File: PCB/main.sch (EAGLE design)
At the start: 18 parts, among them IC1 DCDC, IC2 A4988BREAKOUT, IC3 A4988BREAKOUT, M1 NEAM17, M2 NEAM17

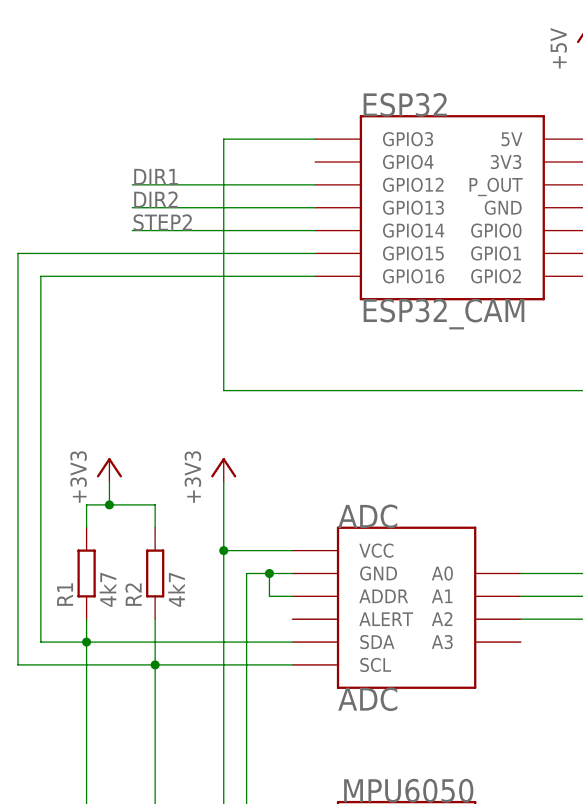
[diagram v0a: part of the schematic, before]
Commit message: PIN 16 is used by PSRAM ...
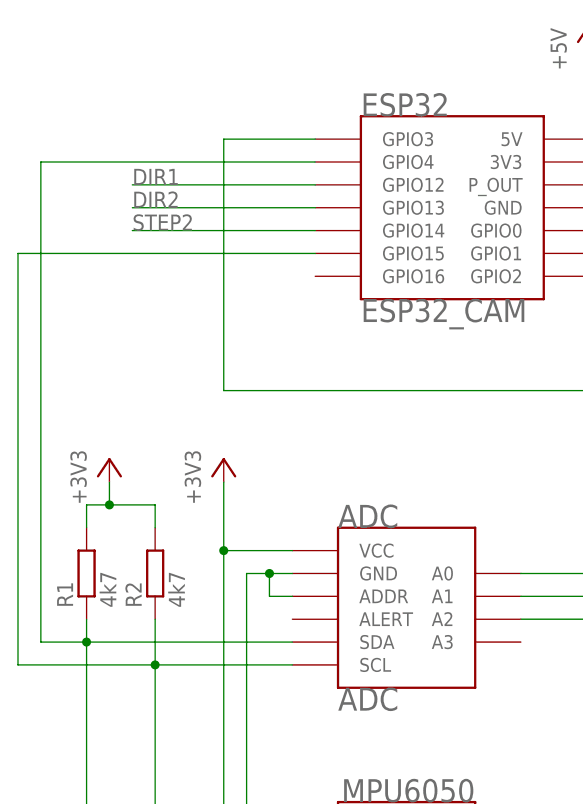
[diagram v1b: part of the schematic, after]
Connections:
- net N$19: now also ESP32.GPIO4; no longer ESP32.GPIO16
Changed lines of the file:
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@@
 <junction x="15.24" y="83.82"/>
 <wire x1="15.24" y1="83.82" x2="10.16" y2="83.82" width="0.1524" layer="91"/>
-<wire x1="10.16" y1="83.82" x2="10.16" y2="124.46" width="0.1524" layer="91"/>
-<pinref part="ESP32" gate="G$1" pin="GPIO16"/>
-<wire x1="10.16" y1="124.46" x2="40.64" y2="124.46" width="0.1524" layer="91"/>
+<wire x1="10.16" y1="83.82" x2="10.16" y2="137.16" width="0.1524" layer="91"/>
+<pinref part="ESP32" gate="G$1" pin="GPIO4"/>
+<wire x1="40.64" y1="137.16" x2="10.16" y2="137.16" width="0.1524" layer="91"/>
 </segment>
 </net>

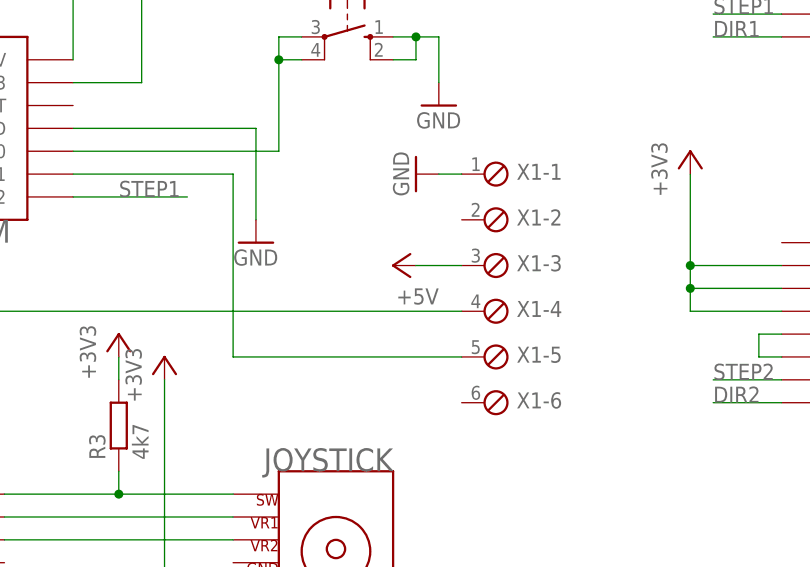
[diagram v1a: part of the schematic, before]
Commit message: change debug port voltage to 3v3
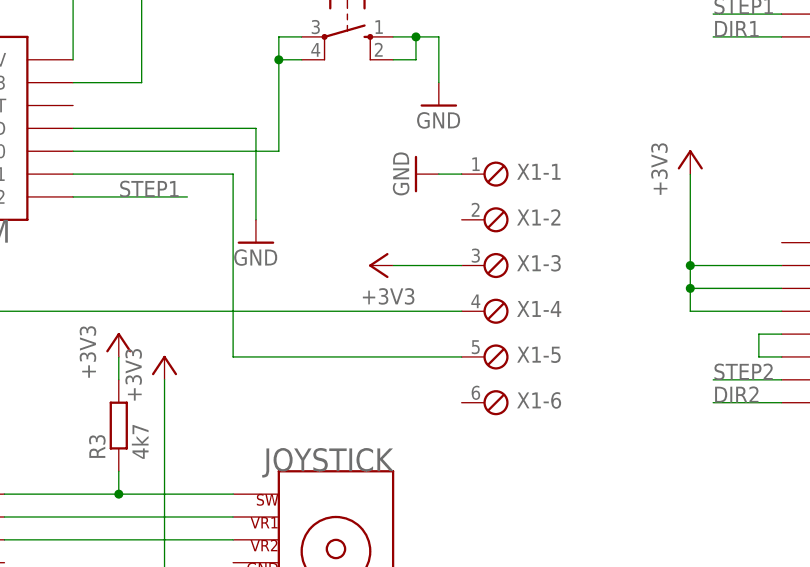
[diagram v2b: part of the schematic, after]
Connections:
- net +3V3: now also X1-3.1
- net +5V: no longer X1-3.1
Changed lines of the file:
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@@
 <part name="X1" library="con-phoenix-254" deviceset="MPT6" device=""/>
 <part name="GND9" library="supply1" deviceset="GND" device=""/>
-<part name="P+6" library="supply1" deviceset="+5V" device=""/>
 <part name="R1" library="rcl" deviceset="R-EU_" device="0207/10" value="4k7"/>
 <part name="R2" library="rcl" deviceset="R-EU_" device="0207/10" value="4k7"/>
@@
 <part name="GND5" library="supply1" deviceset="GND" device=""/>
 <part name="GND11" library="supply1" deviceset="GND" device=""/>
+<part name="+3V2" library="supply1" deviceset="+3V3" device=""/>
 </parts>
 <sheets>
@@
 <instance part="X1" gate="-6" x="116.84" y="101.6"/>
 <instance part="GND9" gate="1" x="109.22" y="127" rot="R270"/>
-<instance part="P+6" gate="1" x="106.68" y="116.84" rot="R90"/>
 <instance part="R1" gate="G$1" x="15.24" y="91.44" rot="R90"/>
 <instance part="R2" gate="G$1" x="22.86" y="91.44" rot="R90"/>
@@
 <instance part="GND5" gate="1" x="210.82" y="116.84"/>
 <instance part="GND11" gate="1" x="210.82" y="157.48"/>
+<instance part="+3V2" gate="G$1" x="104.14" y="116.84" rot="R90"/>
 </instances>
 <busses>
@@
 <pinref part="ESP32" gate="G$1" pin="5V"/>
 </segment>
-<segment>
-<pinref part="X1" gate="-3" pin="1"/>
-<pinref part="P+6" gate="1" pin="+5V"/>
-<wire x1="114.3" y1="116.84" x2="109.22" y2="116.84" width="0.1524" layer="91"/>
-</segment>
 </net>
 <net name="+3V3" class="0">
@@
 <junction x="17.78" y="99.06"/>
 </segment>
+<segment>
+<pinref part="X1" gate="-3" pin="1"/>
+<pinref part="+3V2" gate="G$1" pin="+3V3"/>
+<wire x1="114.3" y1="116.84" x2="106.68" y2="116.84" width="0.1524" layer="91"/>
+</segment>
 </net>

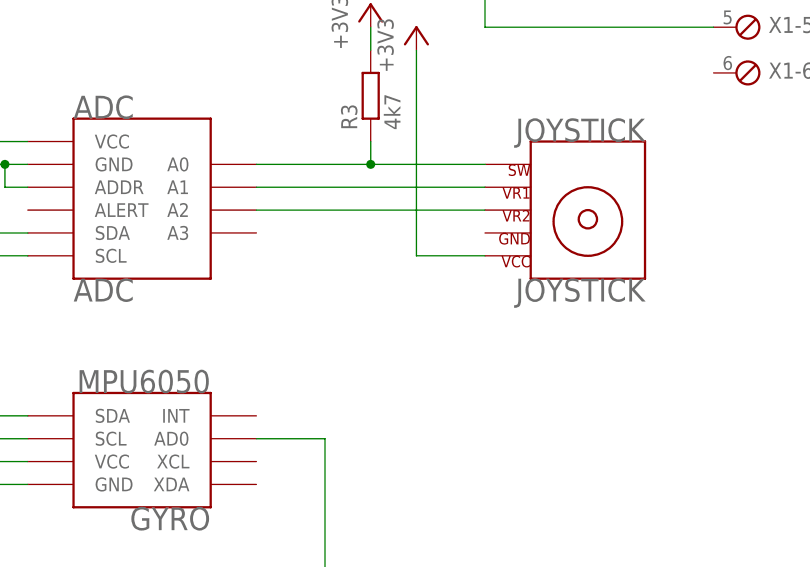
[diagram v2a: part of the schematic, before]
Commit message: Added missing ground connection on the jostick
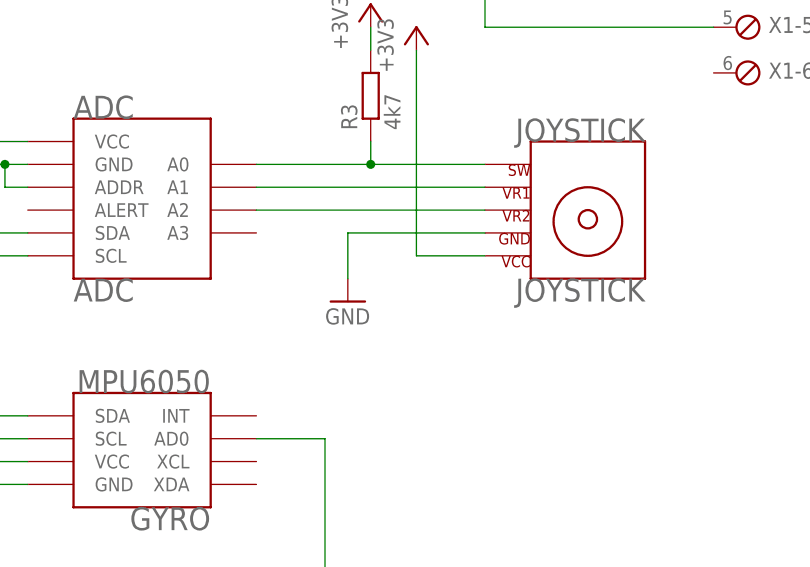
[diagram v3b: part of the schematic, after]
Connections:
- net GND: now also JOYSTICK.GND
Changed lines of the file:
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@@
 <part name="GND11" library="supply1" deviceset="GND" device=""/>
 <part name="+3V2" library="supply1" deviceset="+3V3" device=""/>
+<part name="GND12" library="supply1" deviceset="GND" device=""/>
 </parts>
 <sheets>
@@
 <instance part="GND11" gate="1" x="210.82" y="157.48"/>
 <instance part="+3V2" gate="G$1" x="104.14" y="116.84" rot="R90"/>
+<instance part="GND12" gate="1" x="73.66" y="76.2"/>
 </instances>
 <busses>
@@
 <pinref part="GND11" gate="1" pin="GND"/>
 </segment>
+<segment>
+<pinref part="GND12" gate="1" pin="GND"/>
+<wire x1="73.66" y1="78.74" x2="73.66" y2="83.82" width="0.1524" layer="91"/>
+<pinref part="JOYSTICK" gate="G$1" pin="GND"/>
+<wire x1="73.66" y1="83.82" x2="88.9" y2="83.82" width="0.1524" layer="91"/>
+</segment>
 </net>

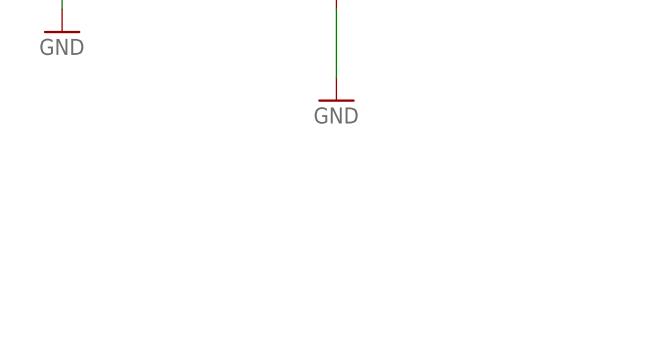
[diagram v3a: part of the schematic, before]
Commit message: lesson learned from prototype
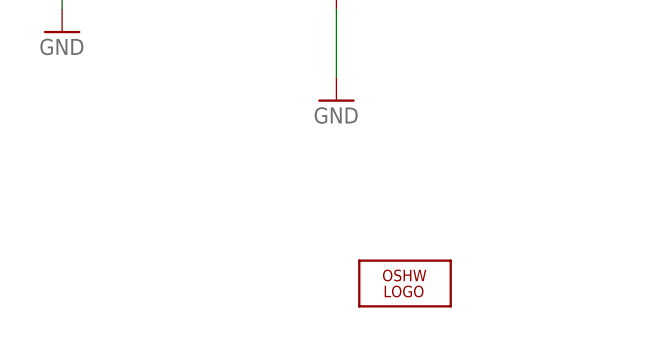
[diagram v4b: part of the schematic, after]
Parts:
- added LOGO1: OHW-LOGO_OSHW_LOGO_FILLX0350-NT, BBLeo_v2:OHW-LOGO_OSHW_LOGO_FILLX0350-NT

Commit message: This is it => V1
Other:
- note added: "(c) im-pro.at"
- note added: "Etch A Selfie"
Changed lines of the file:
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@@
 <grid distance="0.1" unitdist="inch" unit="inch" style="lines" multiple="1" display="no" altdistance="0.01" altunitdist="inch" altunit="inch"/>
 <layers>
-<layer number="1" name="Top" color="4" fill="1" visible="yes" active="no"/>
-<layer number="2" name="Route2" color="1" fill="3" visible="yes" active="no"/>
-<layer number="3" name="Route3" color="4" fill="3" visible="yes" active="no"/>
-<layer number="4" name="Route4" color="1" fill="4" visible="yes" active="no"/>
-<layer number="5" name="Route5" color="4" fill="4" visible="yes" active="no"/>
-<layer number="6" name="Route6" color="1" fill="8" visible="yes" active="no"/>
-<layer number="7" name="Route7" color="4" fill="8" visible="yes" active="no"/>
-<layer number="8" name="Route8" color="1" fill="2" visible="yes" active="no"/>
-<layer number="9" name="Route9" color="4" fill="2" visible="yes" active="no"/>
-<layer number="10" name="Route10" color="1" fill="7" visible="yes" active="no"/>
-<layer number="11" name="Route11" color="4" fill="7" visible="yes" active="no"/>
-<layer number="12" name="Route12" color="1" fill="5" visible="yes" active="no"/>
-<layer number="13" name="Route13" color="4" fill="5" visible="yes" active="no"/>
-<layer number="14" name="Route14" color="1" fill="6" visible="yes" active="no"/>
-<layer number="15" name="Route15" color="4" fill="6" visible="yes" active="no"/>
-<layer number="16" name="Bottom" color="1" fill="1" visible="yes" active="no"/>
-<layer number="17" name="Pads" color="2" fill="1" visible="yes" active="no"/>
-<layer number="18" name="Vias" color="2" fill="1" visible="yes" active="no"/>
-<layer number="19" name="Unrouted" color="6" fill="1" visible="yes" active="no"/>
-<layer number="20" name="Dimension" color="15" fill="1" visible="yes" active="no"/>
-<layer number="21" name="tPlace" color="7" fill="1" visible="yes" active="no"/>
-<layer number="22" name="bPlace" color="7" fill="1" visible="yes" active="no"/>
-<layer number="23" name="tOrigins" color="15" fill="1" visible="yes" active="no"/>
-<layer number="24" name="bOrigins" color="15" fill="1" visible="yes" active="no"/>
-<layer number="25" name="tNames" color="7" fill="1" visible="yes" active="no"/>
-<layer number="26" name="bNames" color="7" fill="1" visible="yes" active="no"/>
-<layer number="27" name="tValues" color="7" fill="1" visible="yes" active="no"/>
-<layer number="28" name="bValues" color="7" fill="1" visible="yes" active="no"/>
+<layer number="1" name="Top" color="4" fill="1" visible="no" active="no"/>
+<layer number="2" name="Route2" color="1" fill="3" visible="no" active="no"/>
+<layer number="3" name="Route3" color="4" fill="3" visible="no" active="no"/>
+<layer number="4" name="Route4" color="1" fill="4" visible="no" active="no"/>
+<layer number="5" name="Route5" color="4" fill="4" visible="no" active="no"/>
+<layer number="6" name="Route6" color="1" fill="8" visible="no" active="no"/>
+<layer number="7" name="Route7" color="4" fill="8" visible="no" active="no"/>
+<layer number="8" name="Route8" color="1" fill="2" visible="no" active="no"/>
+<layer number="9" name="Route9" color="4" fill="2" visible="no" active="no"/>
+<layer number="10" name="Route10" color="1" fill="7" visible="no" active="no"/>
+<layer number="11" name="Route11" color="4" fill="7" visible="no" active="no"/>
+<layer number="12" name="Route12" color="1" fill="5" visible="no" active="no"/>
+<layer number="13" name="Route13" color="4" fill="5" visible="no" active="no"/>
+<layer number="14" name="Route14" color="1" fill="6" visible="no" active="no"/>
+<layer number="15" name="Route15" color="4" fill="6" visible="no" active="no"/>
+<layer number="16" name="Bottom" color="1" fill="1" visible="no" active="no"/>
+<layer number="17" name="Pads" color="2" fill="1" visible="no" active="no"/>
+<layer number="18" name="Vias" color="2" fill="1" visible="no" active="no"/>
+<layer number="19" name="Unrouted" color="6" fill="1" visible="no" active="no"/>
+<layer number="20" name="Dimension" color="15" fill="1" visible="no" active="no"/>
+<layer number="21" name="tPlace" color="7" fill="1" visible="no" active="no"/>
+<layer number="22" name="bPlace" color="7" fill="1" visible="no" active="no"/>
+<layer number="23" name="tOrigins" color="15" fill="1" visible="no" active="no"/>
+<layer number="24" name="bOrigins" color="15" fill="1" visible="no" active="no"/>
+<layer number="25" name="tNames" color="7" fill="1" visible="no" active="no"/>
+<layer number="26" name="bNames" color="7" fill="1" visible="no" active="no"/>
+<layer number="27" name="tValues" color="7" fill="1" visible="no" active="no"/>
+<layer number="28" name="bValues" color="7" fill="1" visible="no" active="no"/>
 <layer number="29" name="tStop" color="7" fill="3" visible="no" active="no"/>
 <layer number="30" name="bStop" color="7" fill="6" visible="no" active="no"/>
@@
 <layer number="35" name="tGlue" color="7" fill="4" visible="no" active="no"/>
 <layer number="36" name="bGlue" color="7" fill="5" visible="no" active="no"/>
-<layer number="37" name="tTest" color="7" fill="1" visible="yes" active="no"/>
-<layer number="38" name="bTest" color="7" fill="1" visible="yes" active="no"/>
+<layer number="37" name="tTest" color="7" fill="1" visible="no" active="no"/>
+<layer number="38" name="bTest" color="7" fill="1" visible="no" active="no"/>
 <layer number="39" name="tKeepout" color="4" fill="11" visible="no" active="no"/>
 <layer number="40" name="bKeepout" color="1" fill="11" visible="no" active="no"/>
@@
 <layer number="44" name="Drills" color="7" fill="1" visible="no" active="no"/>
 <layer number="45" name="Holes" color="7" fill="1" visible="no" active="no"/>
-<layer number="46" name="Milling" color="3" fill="1" visible="yes" active="no"/>
-<layer number="47" name="Measures" color="7" fill="1" visible="yes" active="no"/>
-<layer number="48" name="Document" color="7" fill="1" visible="yes" active="no"/>
-<layer number="49" name="Reference" color="7" fill="1" visible="yes" active="no"/>
-<layer number="50" name="dxf" color="7" fill="1" visible="yes" active="no"/>
-<layer number="51" name="tDocu" color="7" fill="1" visible="yes" active="no"/>
-<layer number="52" name="bDocu" color="7" fill="1" visible="yes" active="no"/>
-<layer number="53" name="tGND_GNDA" color="7" fill="1" visible="yes" active="no"/>
-<layer number="54" name="bGND_GNDA" color="7" fill="1" visible="yes" active="no"/>
-<layer number="56" name="wert" color="7" fill="1" visible="yes" active="no"/>
+<layer number="46" name="Milling" color="3" fill="1" visible="no" active="no"/>
+<layer number="47" name="Measures" color="7" fill="1" visible="no" active="no"/>
+<layer number="48" name="Document" color="7" fill="1" visible="no" active="no"/>
+<layer number="49" name="Reference" color="7" fill="1" visible="no" active="no"/>
+<layer number="50" name="dxf" color="7" fill="1" visible="no" active="no"/>
+<layer number="51" name="tDocu" color="7" fill="1" visible="no" active="no"/>
+<layer number="52" name="bDocu" color="7" fill="1" visible="no" active="no"/>
+<layer number="53" name="tGND_GNDA" color="7" fill="1" visible="no" active="no"/>
+<layer number="54" name="bGND_GNDA" color="7" fill="1" visible="no" active="no"/>
+<layer number="56" name="wert" color="7" fill="1" visible="no" active="no"/>
 <layer number="91" name="Nets" color="2" fill="1" visible="yes" active="yes"/>
 <layer number="92" name="Busses" color="1" fill="1" visible="yes" active="yes"/>
@@
 <plain>
 <text x="99.06" y="152.4" size="1.778" layer="97">BOOT</text>
+<text x="167.64" y="10.16" size="5.08" layer="97">Etch A Selfie</text>
+<text x="218.44" y="20.32" size="1.778" layer="97">(c) im-pro.at</text>
 </plain>
 <instances>
